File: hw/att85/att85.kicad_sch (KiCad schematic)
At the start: 30 parts, among them J101 Barrel_Jack_Switch, J102 Screw_Terminal_01x03, J103 AVR-ISP-6, Q101 BC817, Q102 BC817, SW101 SW_Push, SW102 SW_Push, SW103 SW_Push, SW104 SW_Push, SW105 SW_Push, SW106 SW_Push, U101 ATtiny85-20P

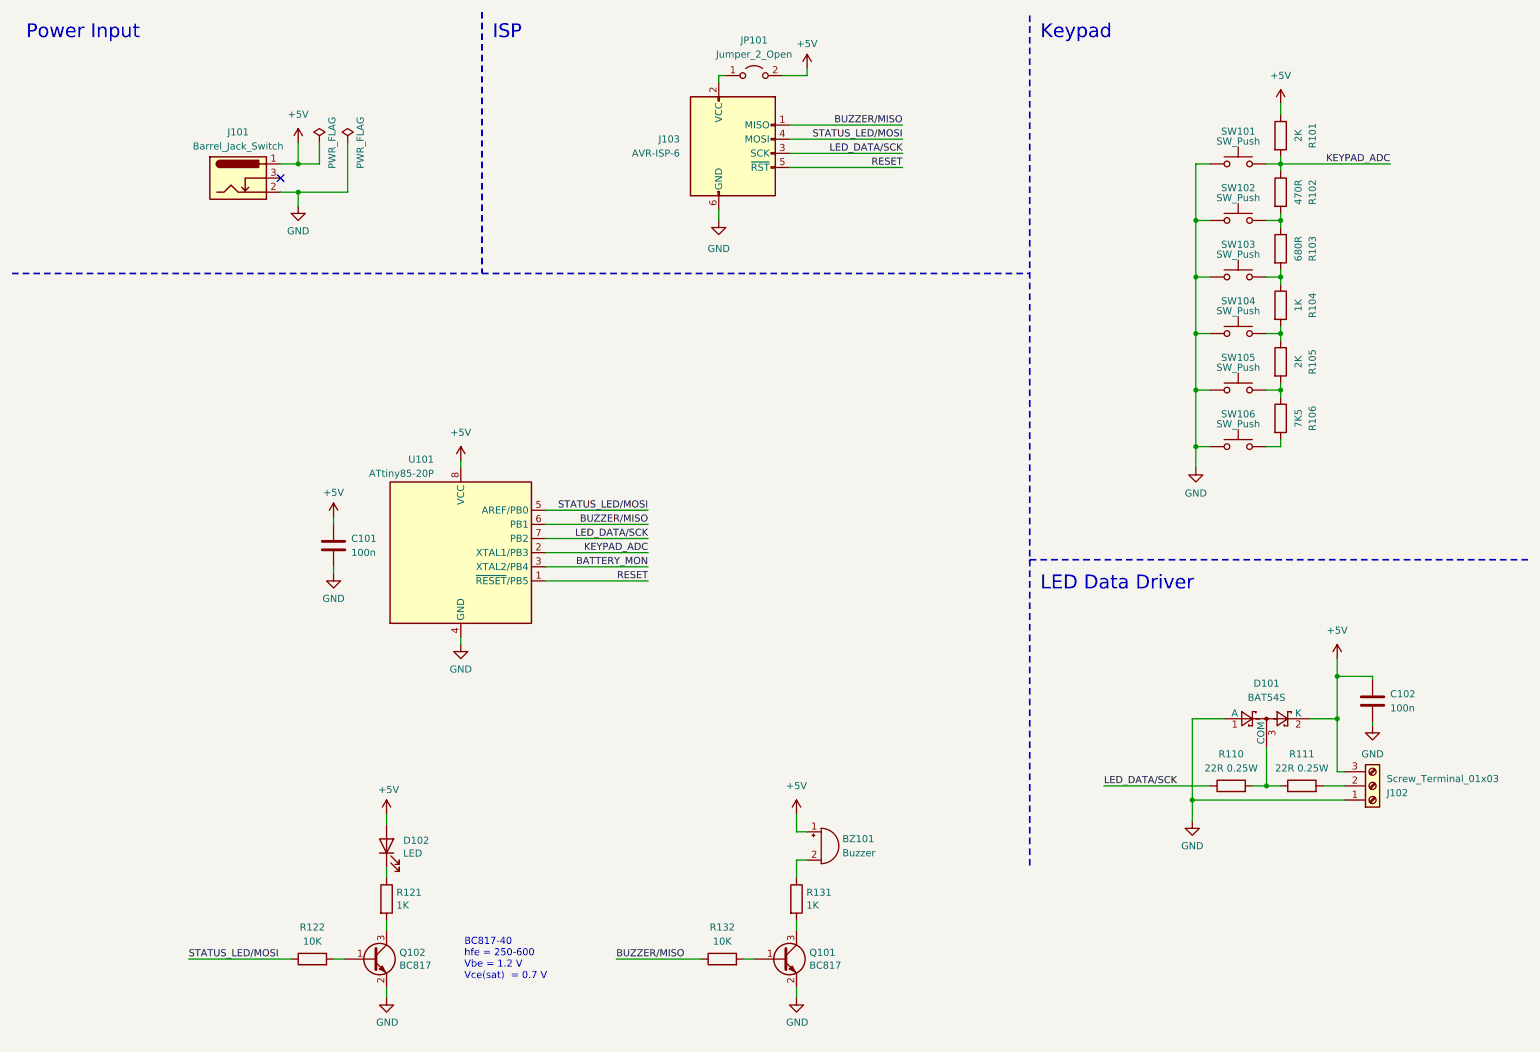
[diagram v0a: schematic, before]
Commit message: chore(hw): add battery power supply
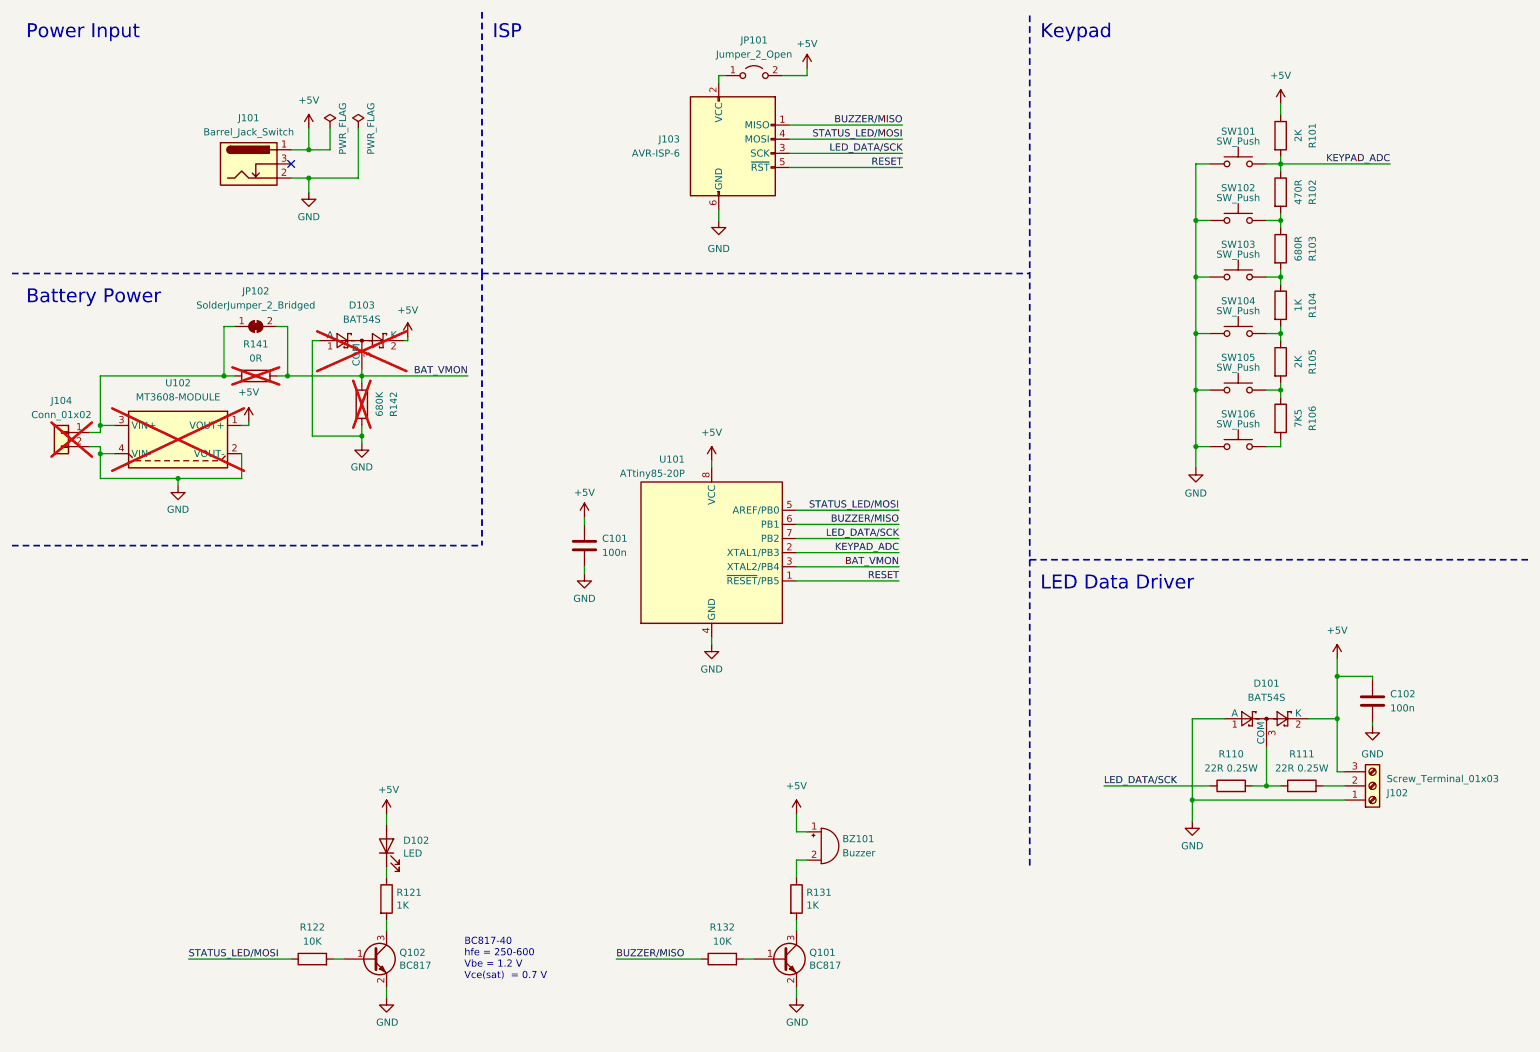
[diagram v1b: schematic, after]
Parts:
- added D103: BAT54S, Package_TO_SOT_SMD:SOT-23, symbol Diode:BAT54S
- added J104: Conn_01x02, Connector_JST:JST_PH_B2B-PH-K_1x02_P2.00mm_Vertical, symbol Connector_Generic:Conn_01x02
- added JP102: SolderJumper_2_Bridged, Jumper:SolderJumper-2_P1.3mm_Bridged_RoundedPad1.0x1.5mm, symbol Jumper:SolderJumper_2_Bridged
- added R141: 0R, Resistor_SMD:R_0805_2012Metric_Pad1.20x1.40mm_HandSolder, symbol Device:R
- added R142: 680K, Resistor_SMD:R_0805_2012Metric_Pad1.20x1.40mm_HandSolder, symbol Device:R
- added U102: MT3608-MODULE, project-specific:mt3608-module, symbol project-specific:mt3608-module
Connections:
- net +5V: now also D103.2 (K), U102.1 (VOUT+)
- net GND: now also D103.1 (A), J104.2 (Pin_2), R142.2, U102.2 (VOUT-), U102.4 (VIN-)
- net BATTERY_MON renamed BAT_VMON
- net BAT_VMON: now also D103.3 (COM), JP102.2 (B), R141.2, R142.1
- new net: J104.1 (Pin_1), JP102.1 (A), R141.1, U102.3 (VIN+)
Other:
- note added: "Battery Power"
- moved on the sheet: C101, J101, U101

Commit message: chore(hw): add communication slot
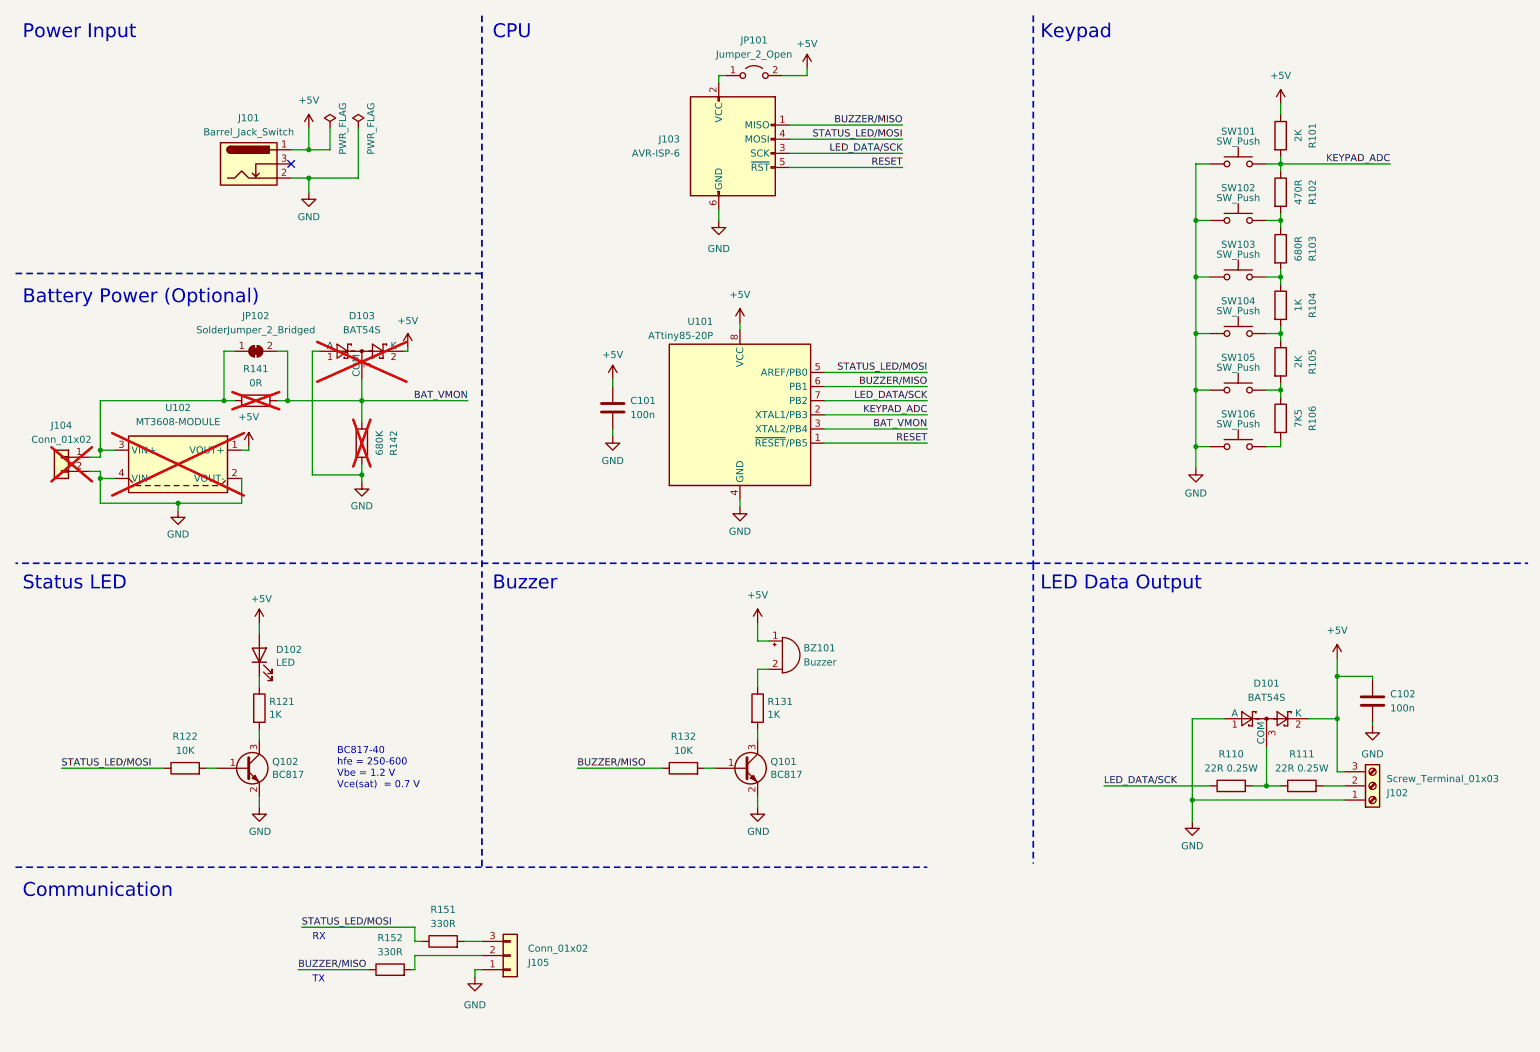
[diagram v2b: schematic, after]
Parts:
- added J105: Conn_01x02, Connector_PinHeader_2.54mm:PinHeader_1x03_P2.54mm_Vertical, symbol Connector_Generic:Conn_01x03
- added R151, R152: 330R, Resistor_SMD:R_0805_2012Metric_Pad1.20x1.40mm_HandSolder, symbol Device:R
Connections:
- net BUZZER/MISO: now also R152.1
- net GND: now also J105.1 (Pin_1)
- net STATUS_LED/MOSI: now also R151.1
- new net: J105.3 (Pin_3), R151.2
- new net: J105.2 (Pin_2), R152.2
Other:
- note added: "Battery Power (Optional)"
- note added: "Buzzer"
- note added: "CPU"
- note added: "Communication"
- note added: "LED Data Output"
- note added: "RX"
- note added: "Status LED"
- note added: "TX"
- note removed: "Battery Power"
- note removed: "ISP"
- note removed: "LED Data Driver"
- moved on the sheet: BZ101, C101, D102, D103, J104, JP102, Q101, Q102, R121, R122, R131, R132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

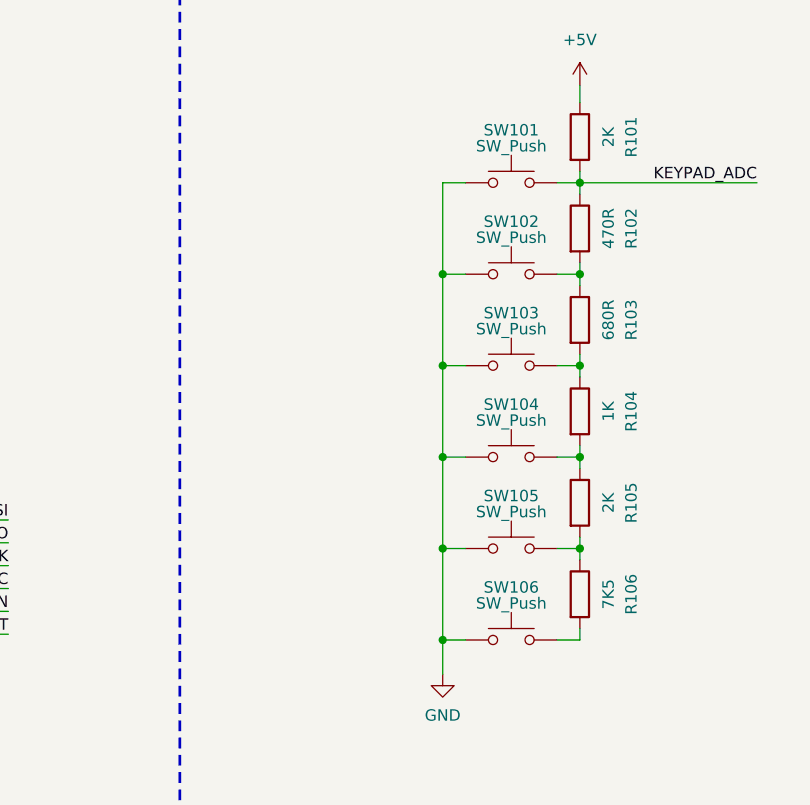
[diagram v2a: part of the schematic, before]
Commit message: chore(hw): finish first version of the layout
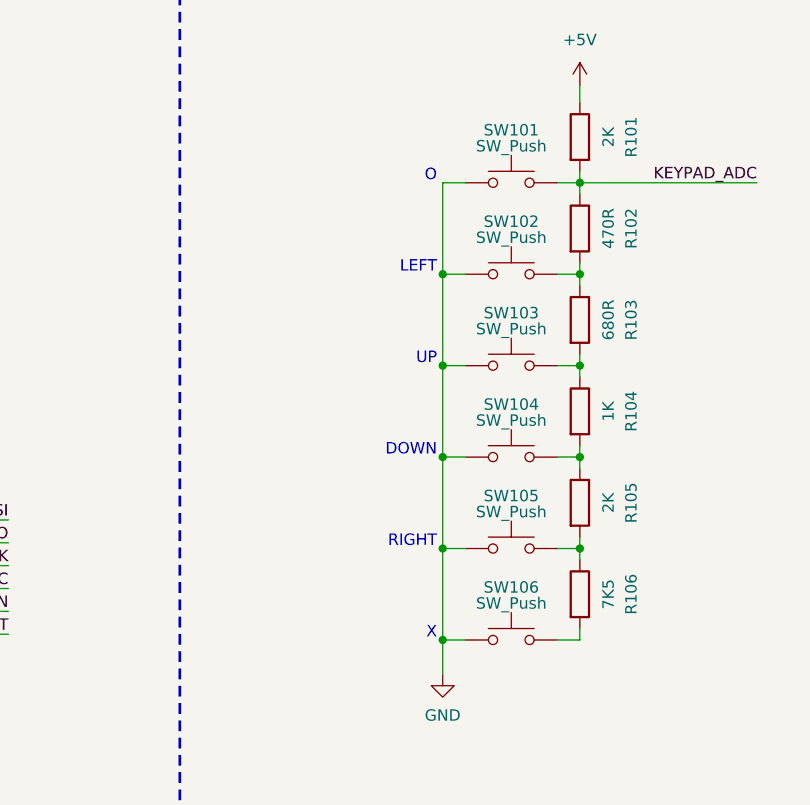
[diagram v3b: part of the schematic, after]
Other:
- note added: "DOWN"
- note added: "LEFT"
- note added: "O"
- note added: "RIGHT"
- note added: "UP"
- note added: "X"
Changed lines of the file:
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@@
     (effects (font (size 2.5 2.5)) (justify left bottom))
+  )
+  (text "RIGHT" (at 224.155 80.01 0)
+    (effects (font (size 1.27 1.27)) (justify right bottom))
   )
   (text "Battery Power (Optional)" (at 13.97 64.77 0)
     (effects (font (size 2.5 2.5)) (justify left bottom))
+  )
+  (text "X" (at 224.155 90.17 0)
+    (effects (font (size 1.27 1.27)) (justify right bottom))
+  )
+  (text "LEFT" (at 224.155 49.53 0)
+    (effects (font (size 1.27 1.27)) (justify right bottom))
+  )
+  (text "UP" (at 224.155 59.69 0)
+    (effects (font (size 1.27 1.27)) (justify right bottom))
   )
   (text "RX" (at 66.04 179.07 0)
@@
   (text "Keypad" (at 196.85 17.145 0)
     (effects (font (size 2.5 2.5)) (justify left bottom))
+  )
+  (text "O" (at 224.155 39.37 0)
+    (effects (font (size 1.27 1.27)) (justify right bottom))
   )
   (text "BC817-40\nhfe = 250-600\nVbe = 1.2 V\nVce(sat)  = 0.7 V"
@@
     (effects (font (size 1.27 1.27)) (justify left bottom))
   )
+  (text "DOWN" (at 224.155 69.85 0)
+    (effects (font (size 1.27 1.27)) (justify right bottom))
+  )
   (text "Buzzer" (at 98.425 116.205 0)

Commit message: chore(hw): improve layout
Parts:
- removed JP102: SolderJumper_2_Bridged, Jumper:SolderJumper-2_P1.3mm_Bridged_RoundedPad1.0x1.5mm, symbol Jumper:SolderJumper_2_Bridged
- R141: footprint Resistor_SMD:R_0805_2012Metric_Pad1.20x1.40mm_HandSolder -> project-specific:R_0805_2012Metric_Pad1.20x1.40mm_HandSolder_Jumper
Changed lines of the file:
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@@
     (comment 1 "www.stefanmisik.com")
   )
-  (junction (at 61.595 81.915) (diameter 0) (color 0 0 0 0)
-  )
   (junction (at 237.49 151.13) (diameter 0) (color 0 0 0 0)
   )
@@
   )
   (junction (at 240.03 49.53) (diameter 0) (color 0 0 0 0)
-  )
-  (junction (at 50.165 81.915) (diameter 0) (color 0 0 0 0)
   )
   (junction (at 250.19 139.065) (diameter 0) (color 0 0 0 0)
@@
     (stroke (width 0) (type default))
   )
-  (wire (pts (xy 27.94 81.915) (xy 50.165 81.915))
-    (stroke (width 0) (type default))
-  )
   (wire (pts (xy 245.11 139.065) (xy 250.19 139.065))
     (stroke (width 0) (type default))
@@
     (stroke (width 0) (type default))
   )
-  (wire (pts (xy 50.165 81.915) (xy 52.07 81.915))
+  (wire (pts (xy 27.94 81.915) (xy 52.07 81.915))
     (stroke (width 0) (type default))
   )
@@
   )
   (wire (pts (xy 27.94 92.075) (xy 27.94 90.805))
-    (stroke (width 0) (type default))
-  )
-  (wire (pts (xy 59.69 81.915) (xy 61.595 81.915))
     (stroke (width 0) (type default))
   )
@@
     (stroke (width 0) (type default))
   )
-  (wire (pts (xy 61.595 73.025) (xy 61.595 81.915))
-    (stroke (width 0) (type default))
-  )
   (wire (pts (xy 54.61 90.805) (xy 54.61 90.17))
     (stroke (width 0) (type default))
@@
     (stroke (width 0) (type default))
   )
-  (wire (pts (xy 50.165 73.025) (xy 50.165 81.915))
-    (stroke (width 0) (type default))
-  )
   (wire (pts (xy 240.03 48.26) (xy 240.03 49.53))
     (stroke (width 0) (type default))
@@
     (stroke (width 0) (type default))
   )
-  (wire (pts (xy 52.07 73.025) (xy 50.165 73.025))
-    (stroke (width 0) (type default))
-  )
   (polyline (pts (xy 195.58 111.125) (xy 12.7 111.125))
     (stroke (width 0.3) (type dash))
@@
     (stroke (width 0.3) (type dash))
   )
-  (wire (pts (xy 61.595 81.915) (xy 74.93 81.915))
+  (wire (pts (xy 59.69 81.915) (xy 74.93 81.915))
     (stroke (width 0) (type default))
   )
@@
   )
   (wire (pts (xy 237.49 80.01) (xy 240.03 80.01))
-    (stroke (width 0) (type default))
-  )
-  (wire (pts (xy 59.69 73.025) (xy 61.595 73.025))
     (stroke (width 0) (type default))
   )
@@
         (path "/fc4ba96f-a9f8-4f1a-a9c5-2b16679a6770"
           (reference "#PWR0119") (unit 1)
-        )
-      )
-    )
-  )
-  (symbol (lib_id "Jumper:SolderJumper_2_Bridged") (at 55.88 73.025 0) (unit 1)
-    (in_bom yes) (on_board yes) (dnp no) (fields_autoplaced)
-    (property "Reference" "JP102" (at 55.88 66.675 0)
-      (effects (font (size 1.27 1.27)))
-    )
-    (property "Value" "SolderJumper_2_Bridged" (at 55.88 69.215 0)
-      (effects (font (size 1.27 1.27)))
-    )
-    (property "Footprint" "Jumper:SolderJumper-2_P1.3mm_Bridged_RoundedPad1.0x1.5mm" (at 55.88 73.025 0)
-      (effects (font (size 1.27 1.27)) hide)
-    )
-    (property "Datasheet" "~" (at 55.88 73.025 0)
-      (effects (font (size 1.27 1.27)) hide)
-    )
-    (pin "1")
-    (pin "2")
-    (instances
-      (project "att85"
-        (path "/fc4ba96f-a9f8-4f1a-a9c5-2b16679a6770"
-          (reference "JP102") (unit 1)
         )
       )
@@
       (effects (font (size 1.27 1.27)))
     )
-    (property "Footprint" "Resistor_SMD:R_0805_2012Metric_Pad1.20x1.40mm_HandSolder" (at 55.88 83.693 90)
-      (effects (font (size 1.27 1.27)) hide)
-    )
+    (property "Footprint" "project-specific:R_0805_2012Metric_Pad1.20x1.40mm_HandSolder_Jumper" (at 55.88 83.693 90)
+      (effects (font (size 1.27 1.27)) hide)
+    )

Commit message: chore(hw): add stacked buzzer footprint
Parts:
- BZ101: footprint Buzzer_Beeper:Buzzer_12x9.5RM7.6 -> project-specific:Buzzer_Stacked
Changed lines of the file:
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@@
       (effects (font (size 1.27 1.27)) (justify left))
     )
-    (property "Footprint" "Buzzer_Beeper:Buzzer_12x9.5RM7.6" (at 149.86 125.095 90)
+    (property "Footprint" "project-specific:Buzzer_Stacked" (at 149.86 125.095 90)
       (effects (font (size 1.27 1.27)) hide)
     )
